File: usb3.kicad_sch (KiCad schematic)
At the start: 46 parts, among them J5 WE_632723300011_alt_symbol, Q4 PJE138K, U17 HD3SS3220, U18 AP22615, U19 TPD4E05U06QDQARQ1, U20 TPD4E05U06QDQARQ1, U21 TPD4E05U06QDQARQ1

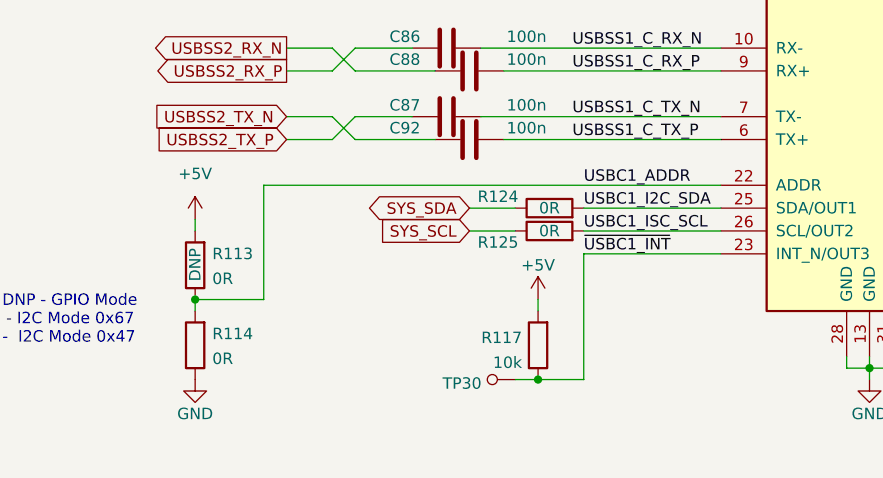
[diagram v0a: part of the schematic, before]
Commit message: Changed configuration pf U17 to GPIO [#40390]
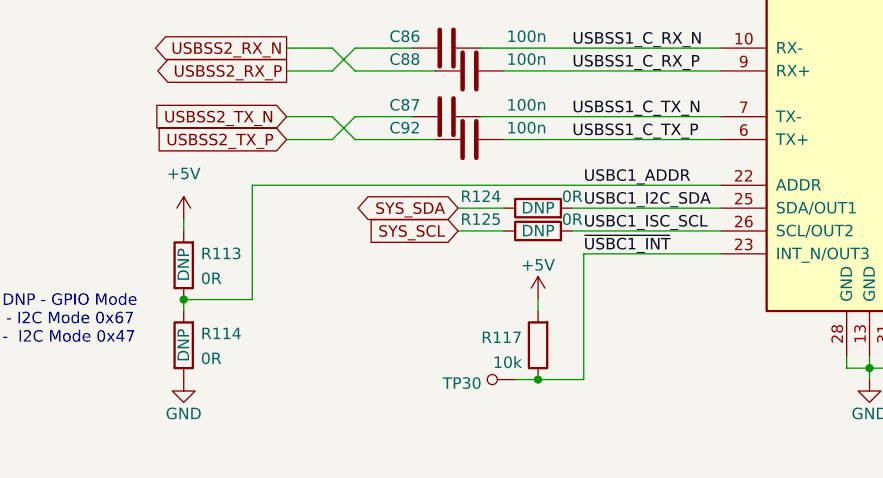
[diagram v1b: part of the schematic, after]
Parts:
- R114, R124, R125: DNP (none) -> DNP
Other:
- moved on the sheet: R113, R114, R124, R125

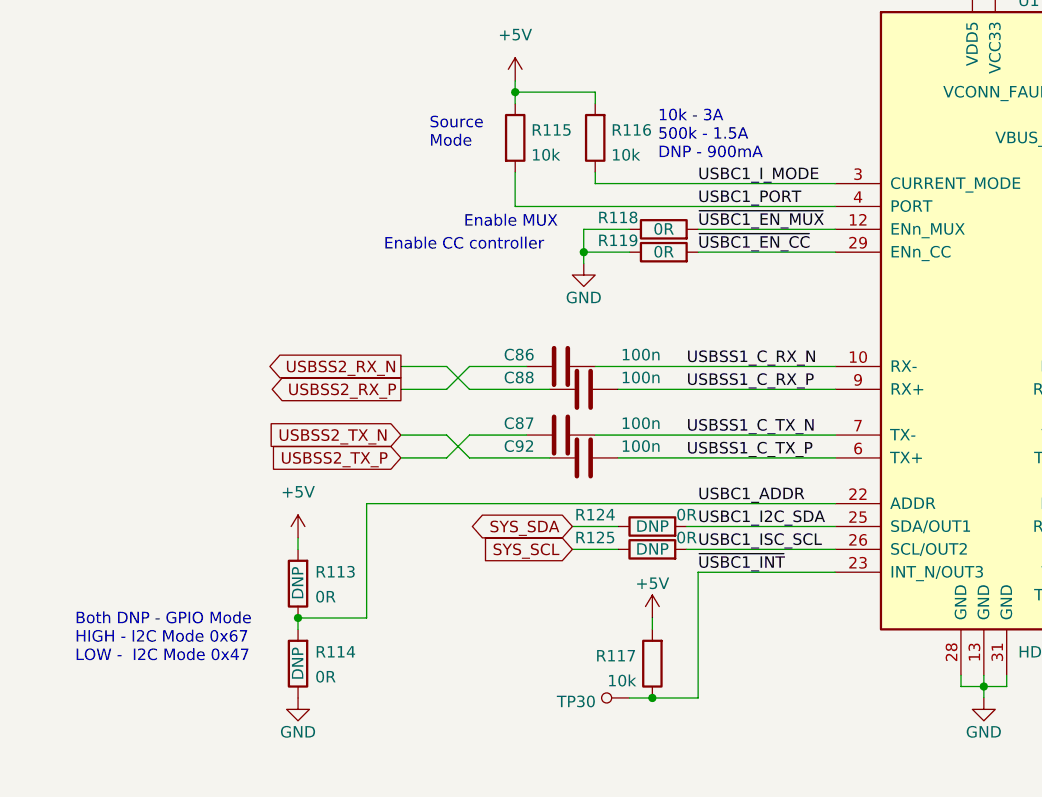
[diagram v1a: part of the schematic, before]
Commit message: Replace USB SS SOM-MUX capacitors with ORs
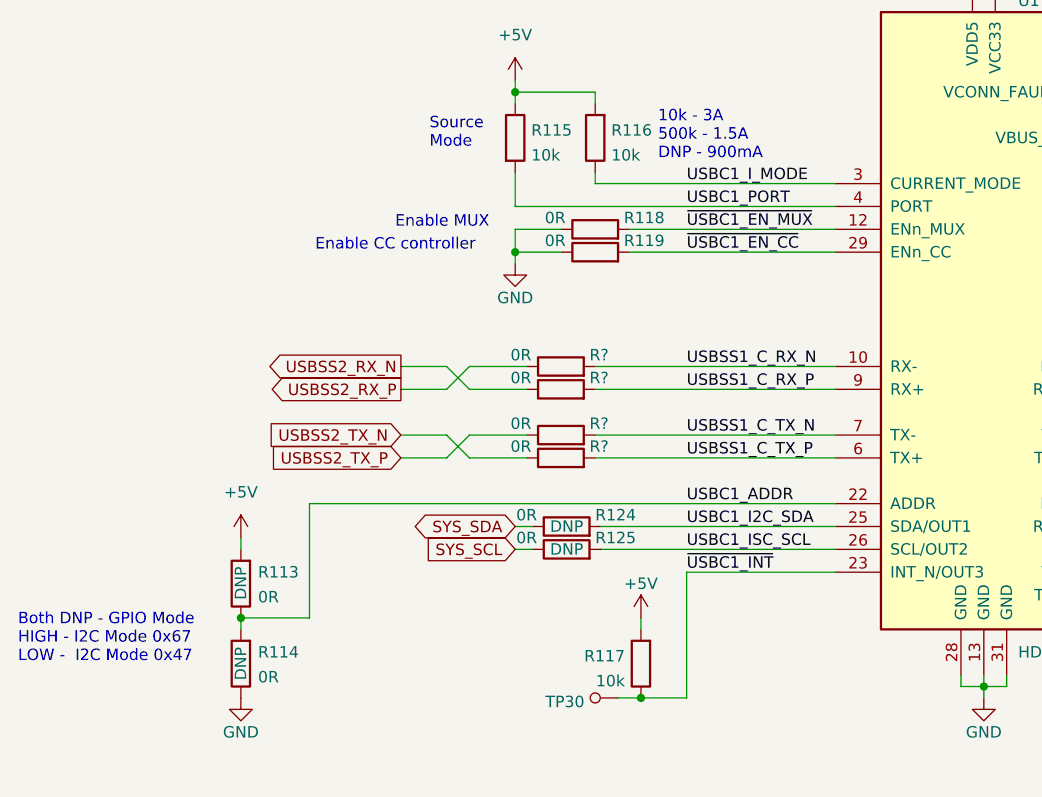
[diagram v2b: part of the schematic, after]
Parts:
- removed C86, C87, C88, C92: C_100n_0402, jetson-orin-baseboard-footprints:0402-cap, symbol jetson-orin-baseboard:C_100n_0402
- added R? (x4): R_0R_0402, jetson-orin-baseboard-footprints:0402-res, symbol jetson-orin-baseboard:R_0R_0402
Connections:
- net USBSS1_C_RX_N: now also R?.2
- net USBSS1_C_RX_P: now also R?.2
- net USBSS1_C_TX_N: now also R?.2
- net USBSS1_C_TX_P: now also R?.2
- net USBSS2_RX_N: now also R?.1
- net USBSS2_RX_P: now also R?.1
- net USBSS2_TX_N: now also R?.1
- net USBSS2_TX_P: now also R?.1
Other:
- moved on the sheet: R113, R114, R117, R118, R119, R124, R125, TP30

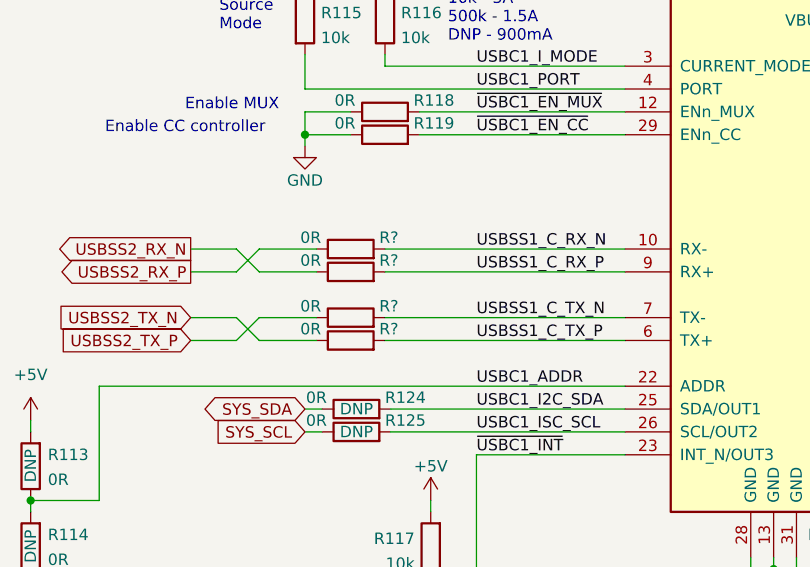
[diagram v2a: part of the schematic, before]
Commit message: Enumerate resistors
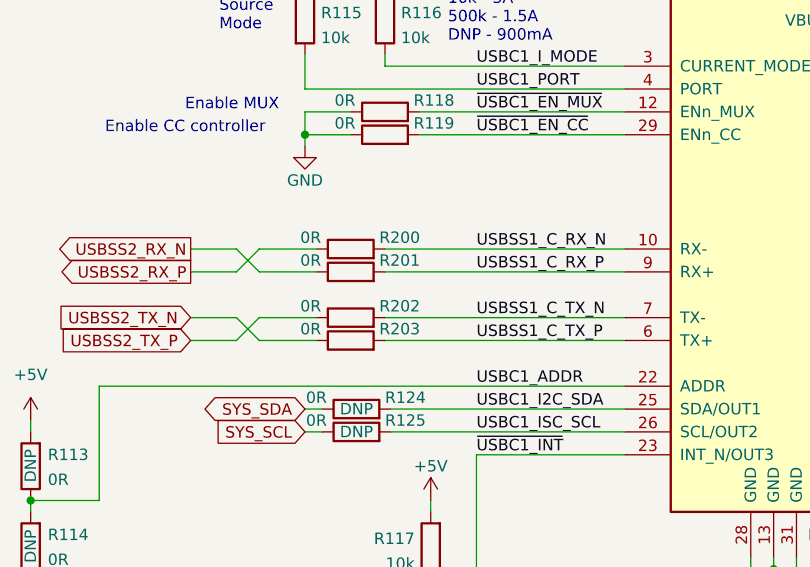
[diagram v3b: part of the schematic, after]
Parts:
- gave numbers to parts that had none: 4
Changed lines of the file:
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@@
   (symbol (lib_id "jetson-orin-baseboard:R_0R_0402") (at 113.03 165.1 0) (unit 1)
     (in_bom yes) (on_board yes)
-    (property "Reference" "R?" (id 0) (at 116.205 163.83 0)
+    (property "Reference" "R203" (id 0) (at 116.205 163.83 0)
       (effects (font (size 1.27 1.27)) (justify left))
     )
@@
   (symbol (lib_id "jetson-orin-baseboard:R_0R_0402") (at 113.03 162.56 0) (unit 1)
     (in_bom yes) (on_board yes)
-    (property "Reference" "R?" (id 0) (at 116.205 161.29 0)
+    (property "Reference" "R202" (id 0) (at 116.205 161.29 0)
       (effects (font (size 1.27 1.27)) (justify left))
     )
@@
   (symbol (lib_id "jetson-orin-baseboard:R_0R_0402") (at 113.03 154.94 0) (unit 1)
     (in_bom yes) (on_board yes)
-    (property "Reference" "R?" (id 0) (at 116.205 153.67 0)
+    (property "Reference" "R200" (id 0) (at 116.205 153.67 0)
       (effects (font (size 1.27 1.27)) (justify left))
     )
@@
   (symbol (lib_id "jetson-orin-baseboard:R_0R_0402") (at 113.03 157.48 0) (unit 1)
     (in_bom yes) (on_board yes)
-    (property "Reference" "R?" (id 0) (at 116.205 156.21 0)
-      (effects (font (size 1.27 1.27)) (justify left))
-    )
+    (property "Reference" "R201" (id 0) (at 116.205 156.21 0)
+      (effects (font (size 1.27 1.27)) (justify left))
+    )

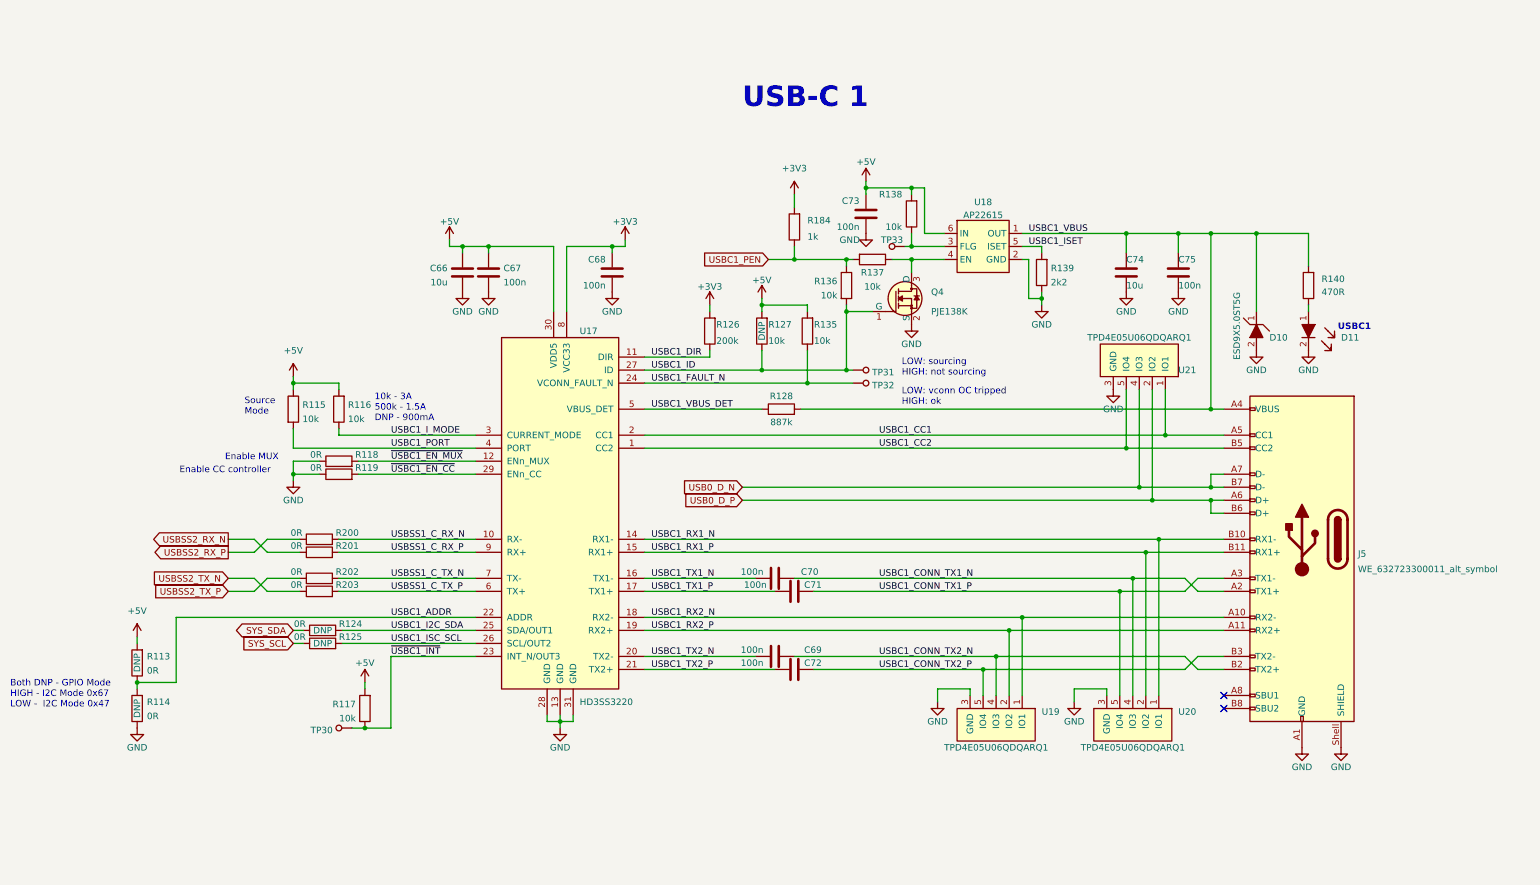
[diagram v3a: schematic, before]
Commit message: Connect USB3 ID detection to GPIO00
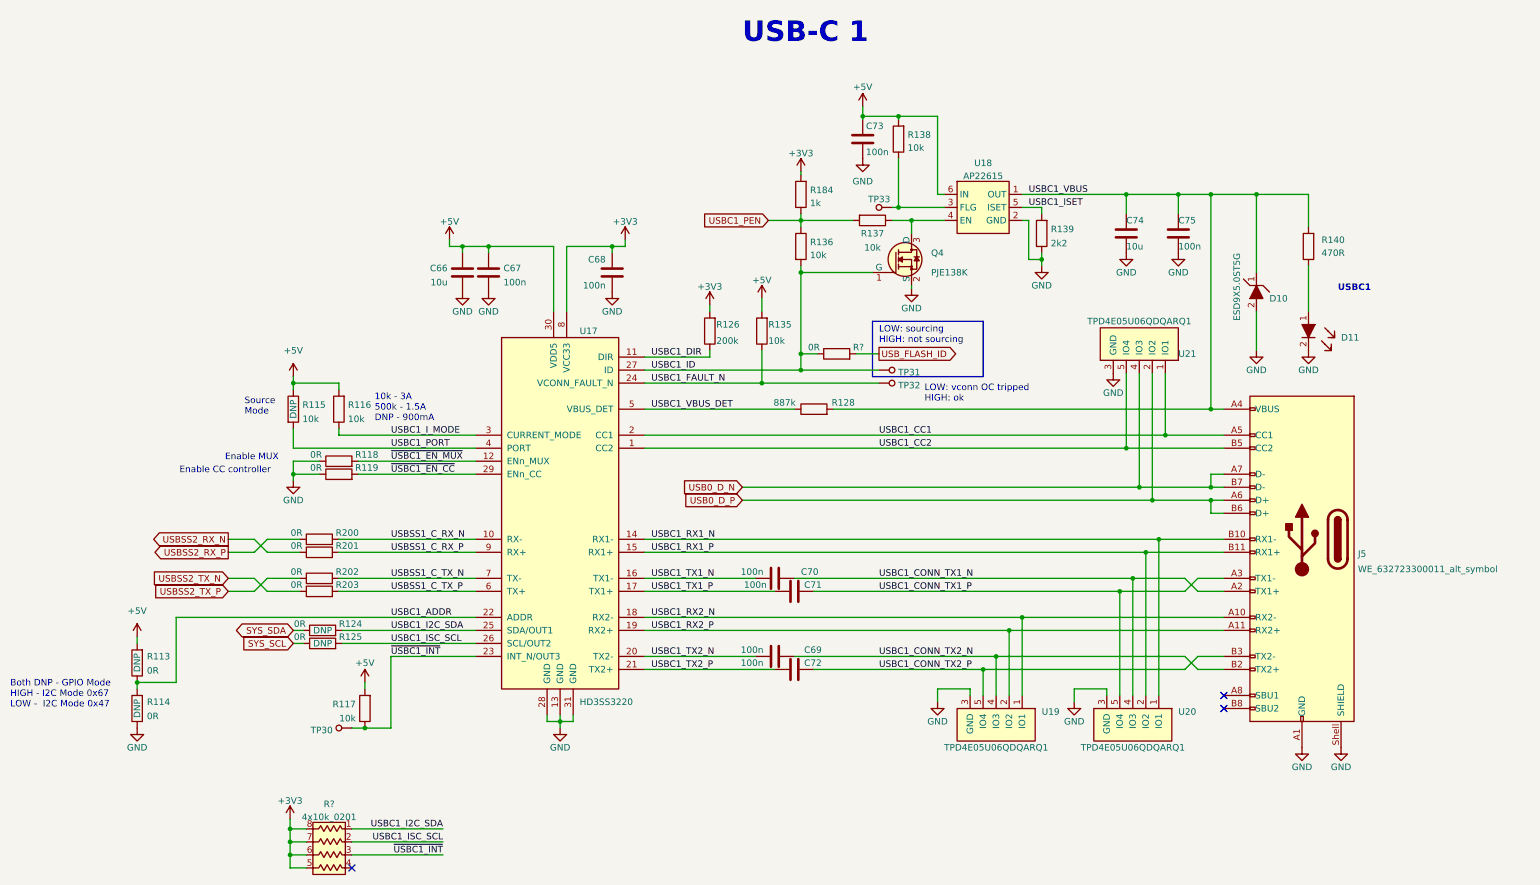
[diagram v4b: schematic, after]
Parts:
- removed R127: R_10k_0402, jetson-orin-baseboard-footprints:0402-res, symbol jetson-orin-baseboard:R_10k_0402
- added R?: 4x10k_0201_array, antmicro-footprints:EXB18V, symbol antmicroResistorNetworksArrays:4x10k_0201_array
- added R?: R_0R_0402, jetson-orin-baseboard-footprints:0402-res, symbol jetson-orin-baseboard:R_0R_0402
- R115: DNP (none) -> DNP
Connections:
- net +3V3: now also R?.5, R?.6, R?.7, R?.8
- net USBC1_I2C_SDA: now also R?.1
- net USBC1_ID: now also R?.1
- net USBC1_ISC_SCL: now also R?.2
- net ~{USBC1_INT}: now also R?.3
- new net USB_FLASH_ID: R?.2
- no-connect marks 2 -> 3
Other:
- moved on the sheet: C73, C74, C75, D10, Q4, R128, R135, R136, R137, R138, R139, R140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

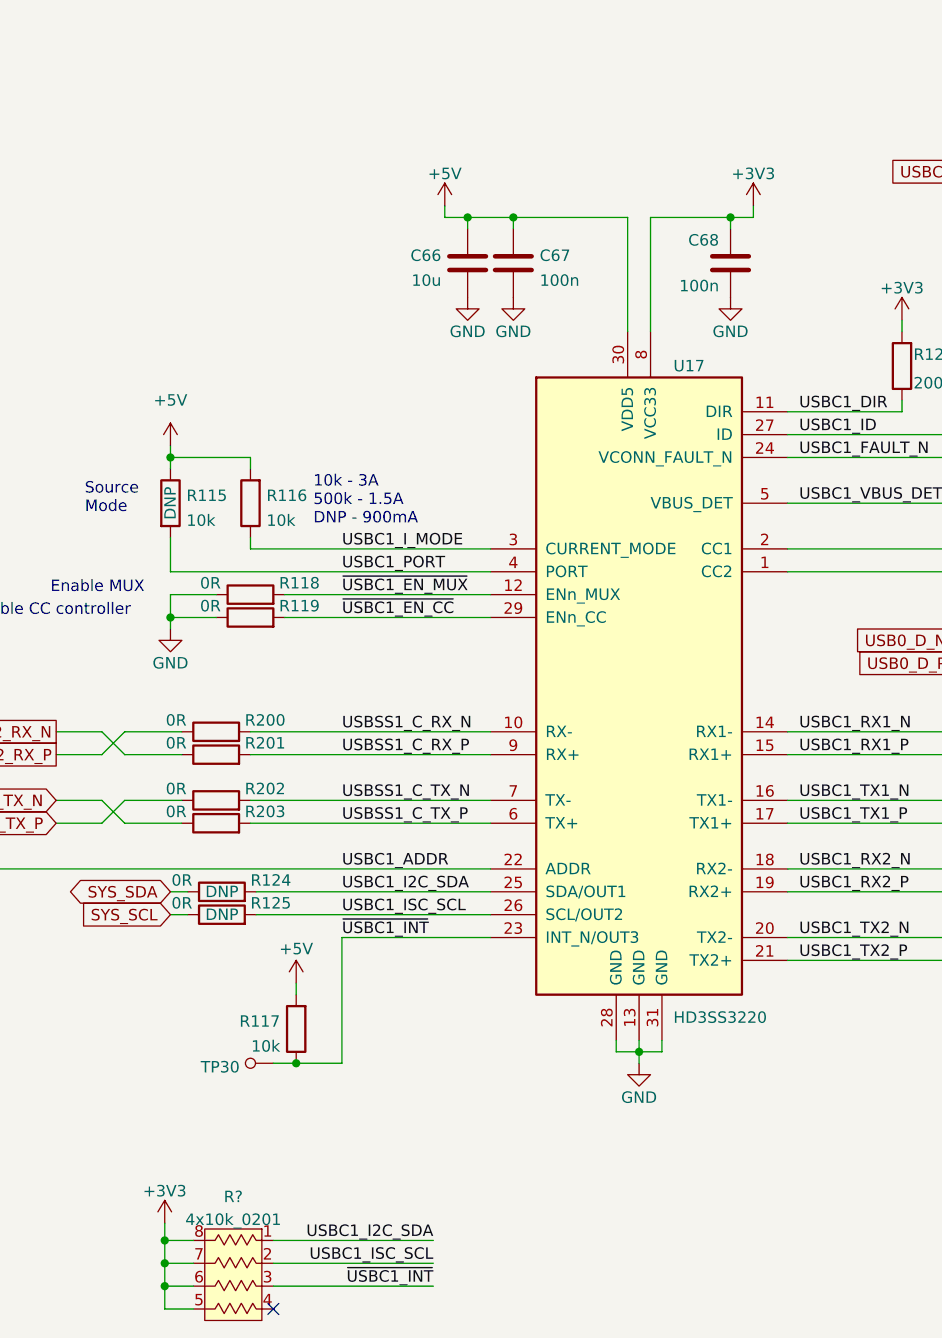
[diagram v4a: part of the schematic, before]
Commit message: Add 220k pullups to HD3SS3220 OUTx pins
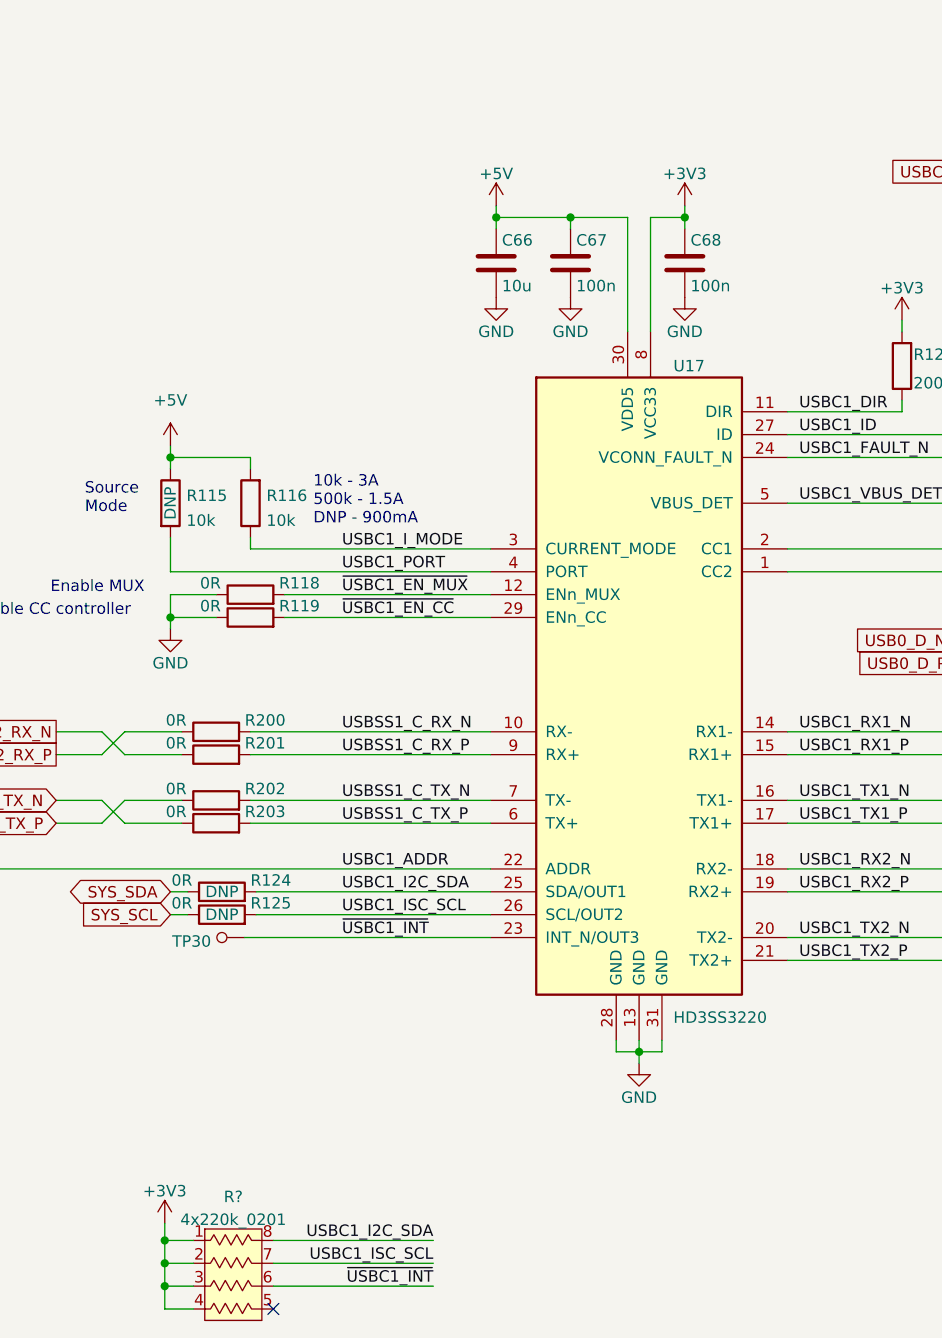
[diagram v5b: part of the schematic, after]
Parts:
- removed R117: R_10k_0402, jetson-orin-baseboard-footprints:0402-res, symbol jetson-orin-baseboard:R_10k_0402
- removed R?: 4x10k_0201_array, antmicro-footprints:EXB18V, symbol antmicroResistorNetworksArrays:4x10k_0201_array
- added R?: 4x220k_0201_array_1, antmicro-footprints:EXB18V, symbol antmicroResistorNetworksArrays:4x220k_0201_array_1
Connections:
- net +3V3: now also R?.1, R?.2, R?.3, R?.4
- net USBC1_I2C_SDA: now also R?.8
- net USBC1_ISC_SCL: now also R?.7
- net ~{USBC1_INT}: now also R?.6
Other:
- moved on the sheet: C66, C67, C68, TP30
